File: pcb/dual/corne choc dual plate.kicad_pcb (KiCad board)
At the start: 2 copper layers, 136.4 x 88.6 mm, 21 parts, among them SW1 SW_PUSH, SW10 SW_PUSH, SW11 SW_PUSH, SW12 SW_PUSH, SW13 SW_PUSH, SW14 SW_PUSH, SW15 SW_PUSH, SW16 SW_PUSH, SW17 SW_PUSH, SW18 SW_PUSH, SW2 SW_PUSH, SW20 SW_PUSH, SW3 SW_PUSH, SW4 SW_PUSH, SW45 SW_PUSH, SW46 SW_PUSH, SW5 SW_PUSH, SW6 SW_PUSH, SW7 SW_PUSH, SW8 SW_PUSH, SW9 SW_PUSH

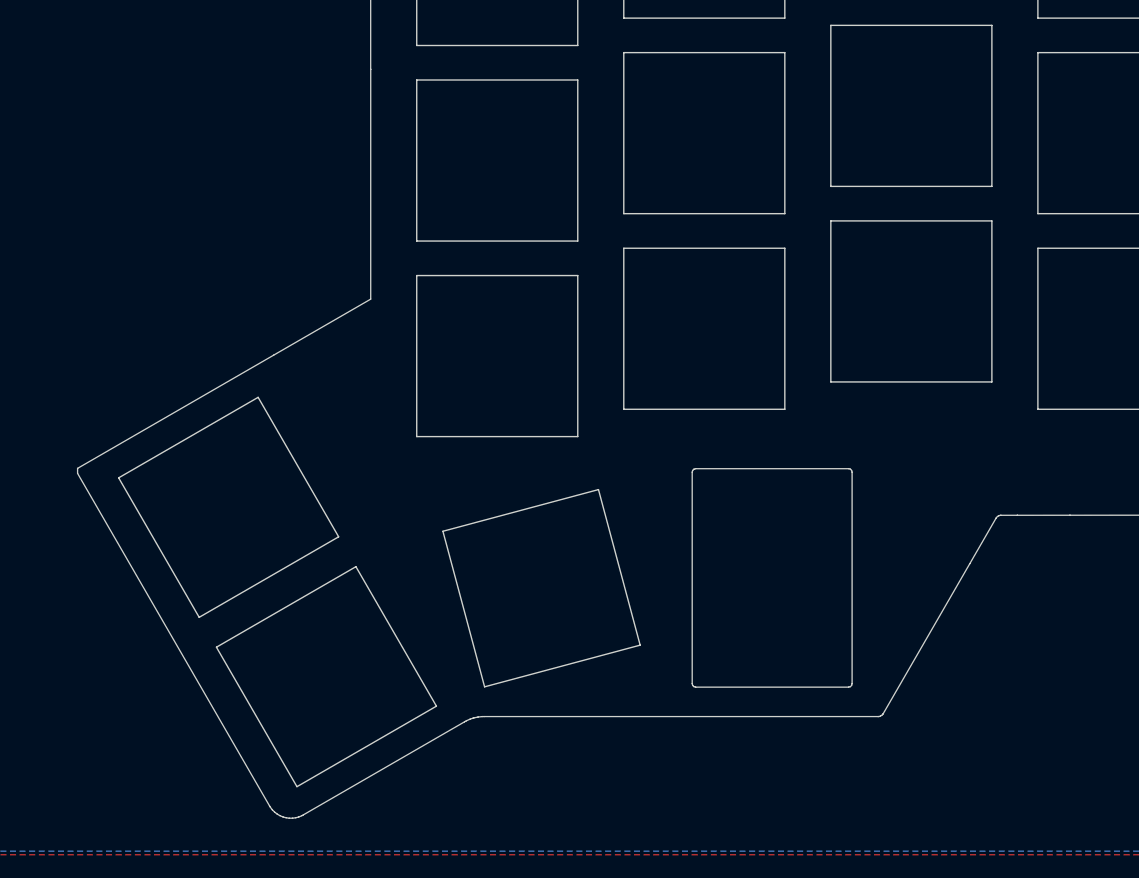
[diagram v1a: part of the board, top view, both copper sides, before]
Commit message: Thumb cluster on the index-aligned arc, wider inner edge, 15-degree marks
- The thumb cluster sits 1.37 mm further in and 0.98 mm higher, so the middle
  thumb key meets the bottom index key the way it meets the inner key (same
  corner gap, opening at 15 degrees); the trackpoint moves with it.
- The inner straight edge moves out by what the upper inner thumb key needs
  to keep the 1.15 mm gap (6.92 mm in all); jacks stay centred in the strip,
  1.24 mm from the controller pins.
- Silkscreen protractor marks ("15°") in the three thumb gaps, on the PCB
  front and both faces of every switch plate.
- Both variants rebuilt; plate renders include silkscreen.
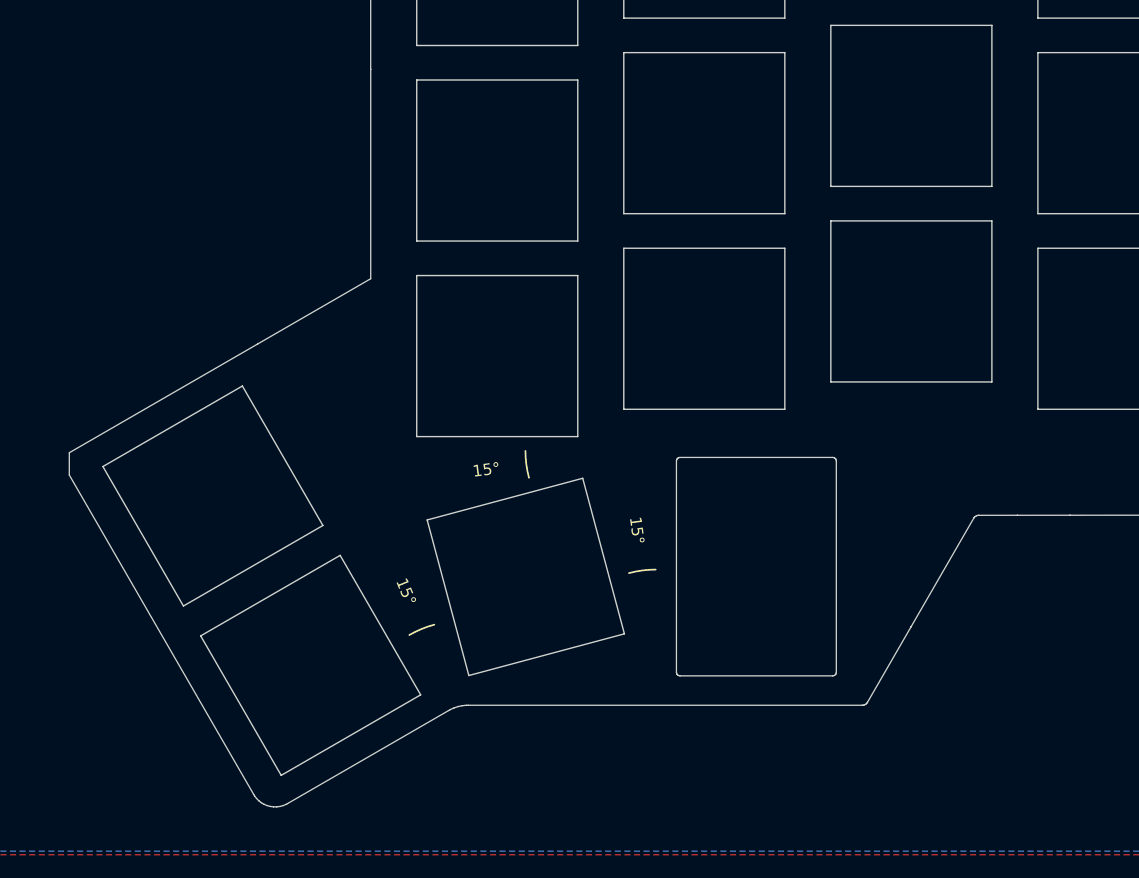
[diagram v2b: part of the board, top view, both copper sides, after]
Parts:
- moved SW20 1.69 mm to (181.3, 119.1)
- moved SW45 1.69 mm to (162.6, 126.8)
- moved SW46 1.69 mm to (154.1, 112.1)
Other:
- board size 136.4 x 88.6 mm -> 137.1 x 87.6 mm
- board text added: "15°"
